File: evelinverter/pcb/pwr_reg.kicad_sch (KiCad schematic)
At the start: 13 parts, among them U6 AP1117-33, U7 TPS62933

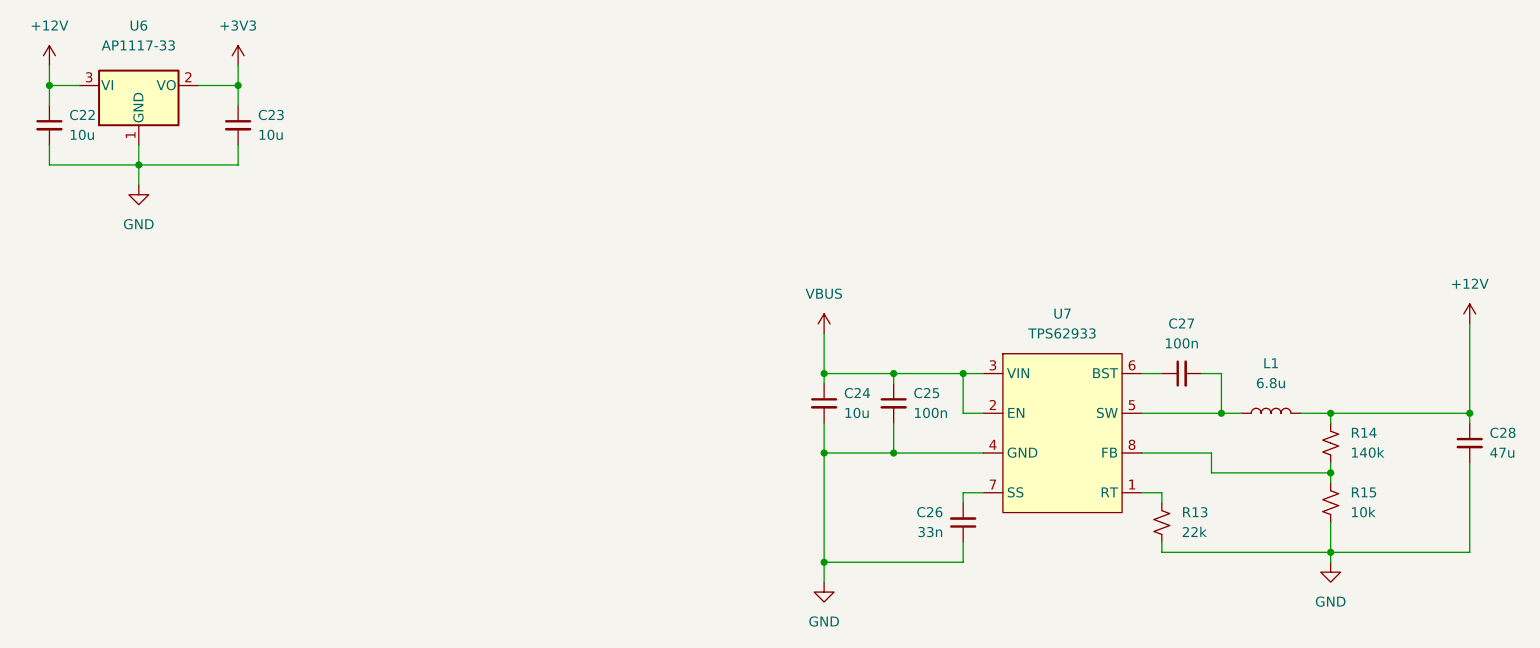
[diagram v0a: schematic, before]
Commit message: started redoing evelinverter
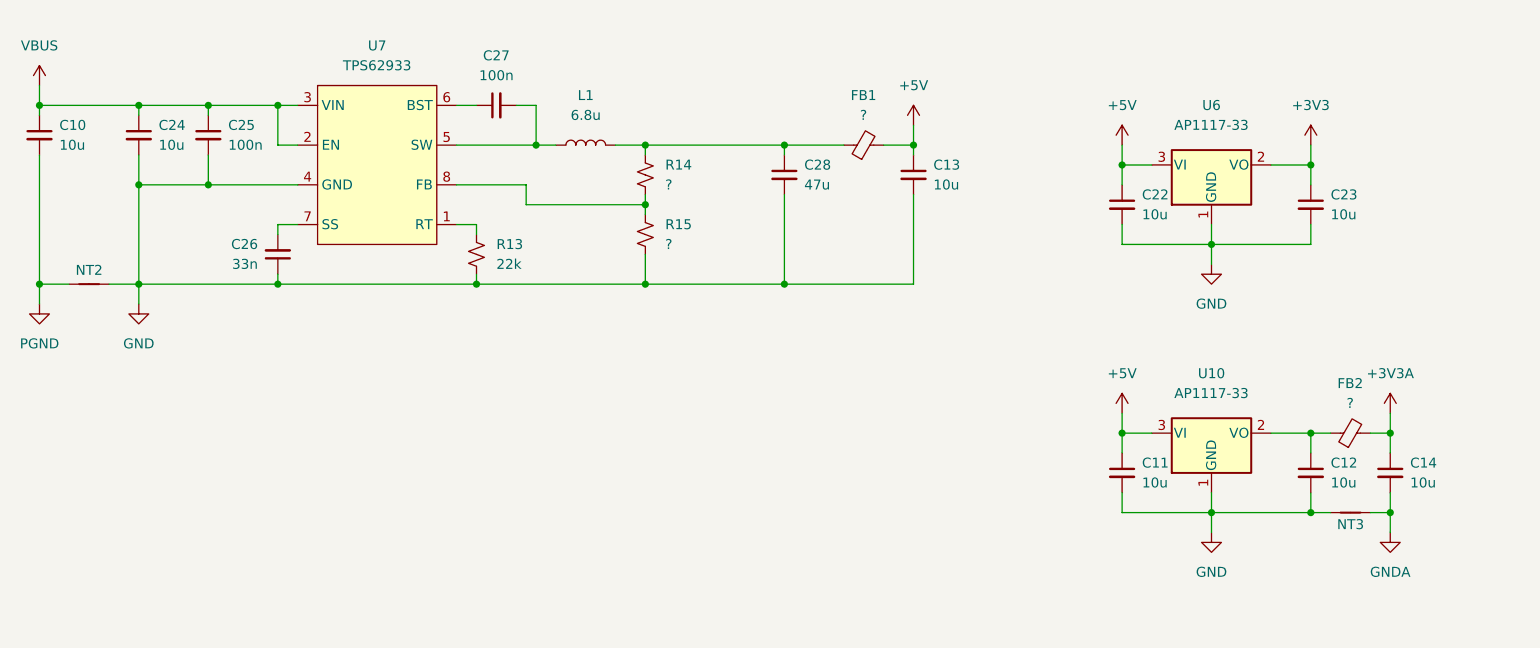
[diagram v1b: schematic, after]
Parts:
- added C10: 10u, Capacitor_SMD:C_1210_3225Metric, symbol Device:C_Small
- added C11, C12, C14: 10u, Capacitor_SMD:C_0603_1608Metric, symbol Device:C_Small
- added C13: 10u, symbol Device:C_Small
- added FB1, FB2: ?, symbol Device:FerriteBead_Small
- added NT2, NT3: NetTie_2, symbol Device:NetTie_2
- added U10: AP1117-33, Package_TO_SOT_SMD:SOT-89-3, symbol Regulator_Linear:AP1117-33
- R14: value 140k -> ?
- R15: value 10k -> ?
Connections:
- net GND: now also C11.2, C12.2, C13.2, NT2.2, NT3.1, U10.1 (GND)
- net VBUS: now also C10.1
- net +12V: no longer names the net of C28.1, L1.2, R14.1
- net +12V: now also FB1.1; no longer C22.1, U6.3 (VI)
- new net: C12.1, FB2.1, U10.2 (VO)
- new net +3V3A: C14.1, FB2.2
- new net +5V: C11.1, C13.1, C22.1, FB1.2, U10.3 (VI), U6.3 (VI)
- new net GNDA: C14.2, NT3.2
- new net PGND: C10.2, NT2.1
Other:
- moved on the sheet: C22, C23, C24, C25, C26, C27, C28, L1, R13, R14, R15, U6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
